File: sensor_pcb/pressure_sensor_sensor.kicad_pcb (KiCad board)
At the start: 2 copper layers, 34 x 34 mm, 12 parts, among them J1 Conn_01x01_Pin, J10 Conn_01x02_Pin, J12 Conn_01x01_Pin, J13 Conn_01x01_Pin, J14 Conn_01x01_Pin, J15 Conn_01x01_Pin, J16 Conn_01x01_Pin, J17 Conn_01x01_Pin, J18 Conn_01x01_Pin, J7 Conn_01x02_Pin, J8 Conn_01x02_Pin, J9 Conn_01x02_Pin

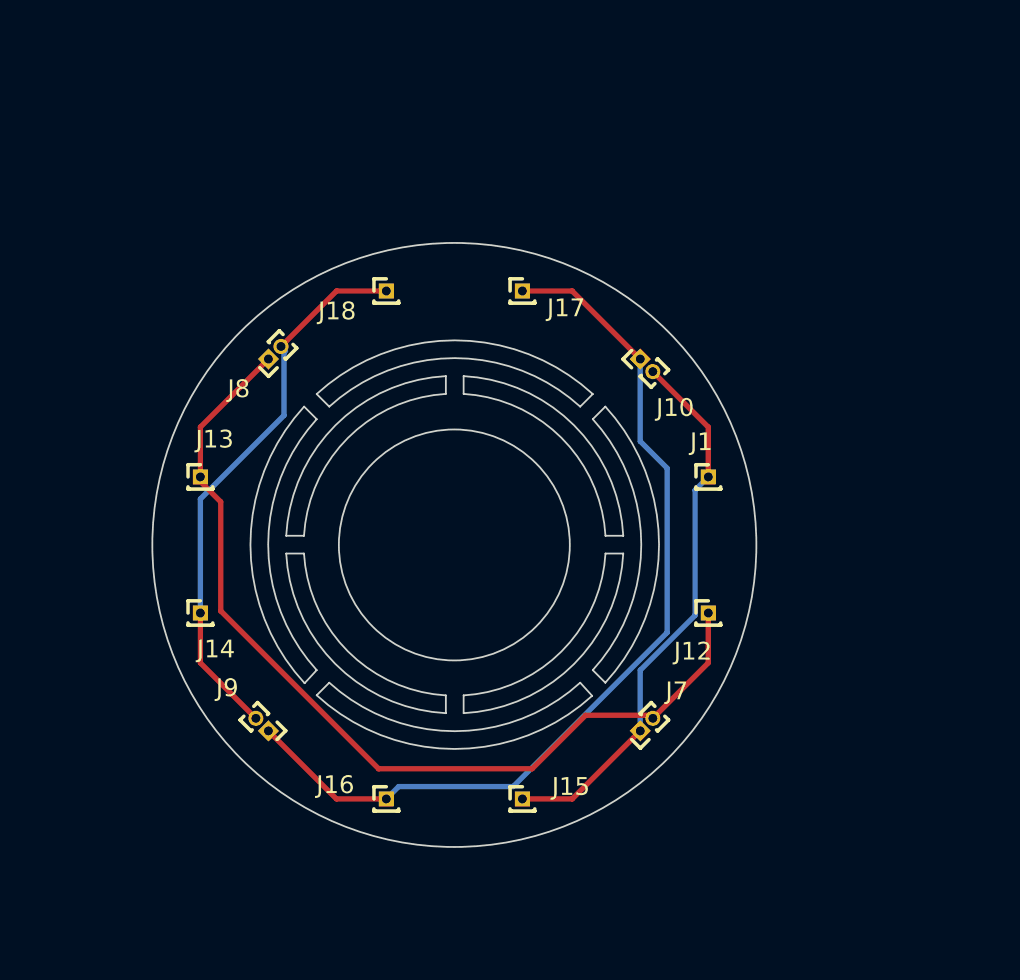
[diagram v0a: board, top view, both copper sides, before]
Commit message: mounting_holes_added
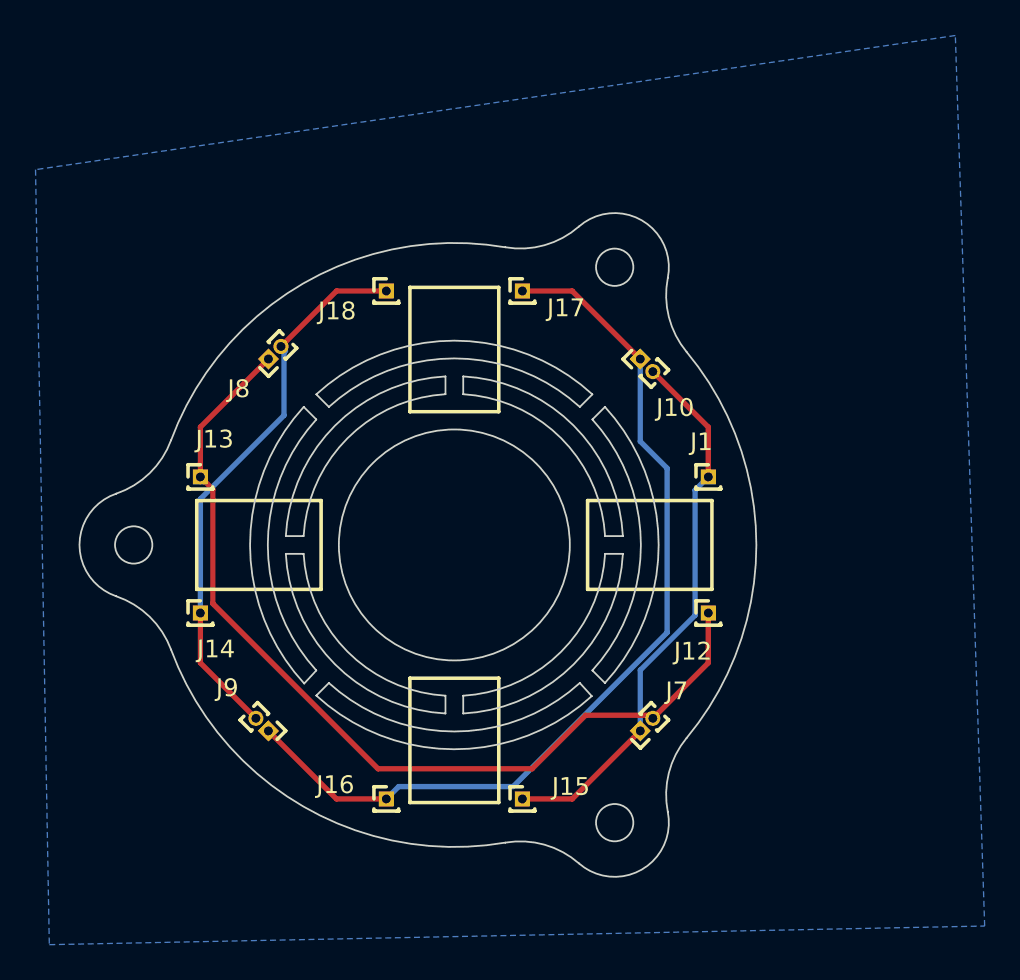
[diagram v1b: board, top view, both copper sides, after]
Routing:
- added copper zone on B.Cu, net GNDA
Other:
- board size 34 x 34 mm -> 38.1 x 37.4 mm

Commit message: alignement_corrected
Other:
- outline, holes or cut-outs redrawn
- board text added: "+3.3V"
- board text added: "A+"
- board text added: "A-"
- board text added: "GND"

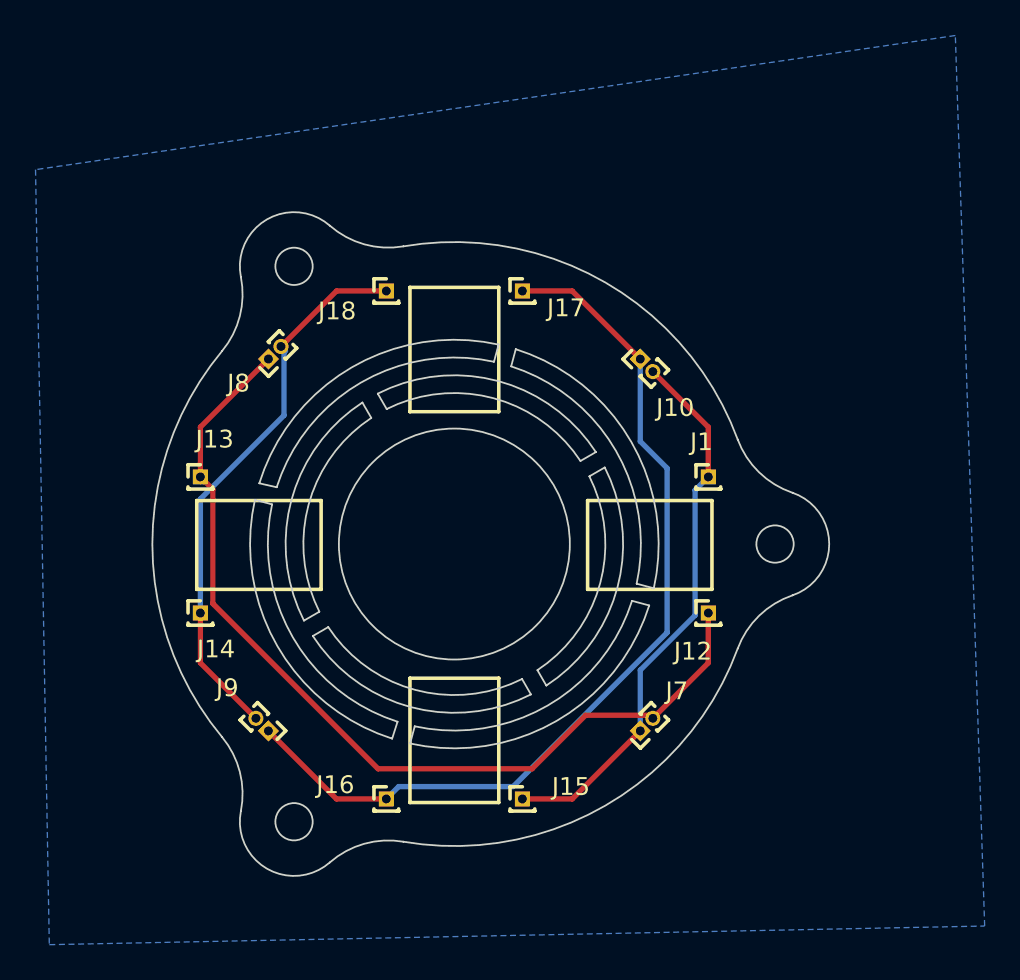
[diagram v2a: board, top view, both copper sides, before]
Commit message: 3d_start_point_added
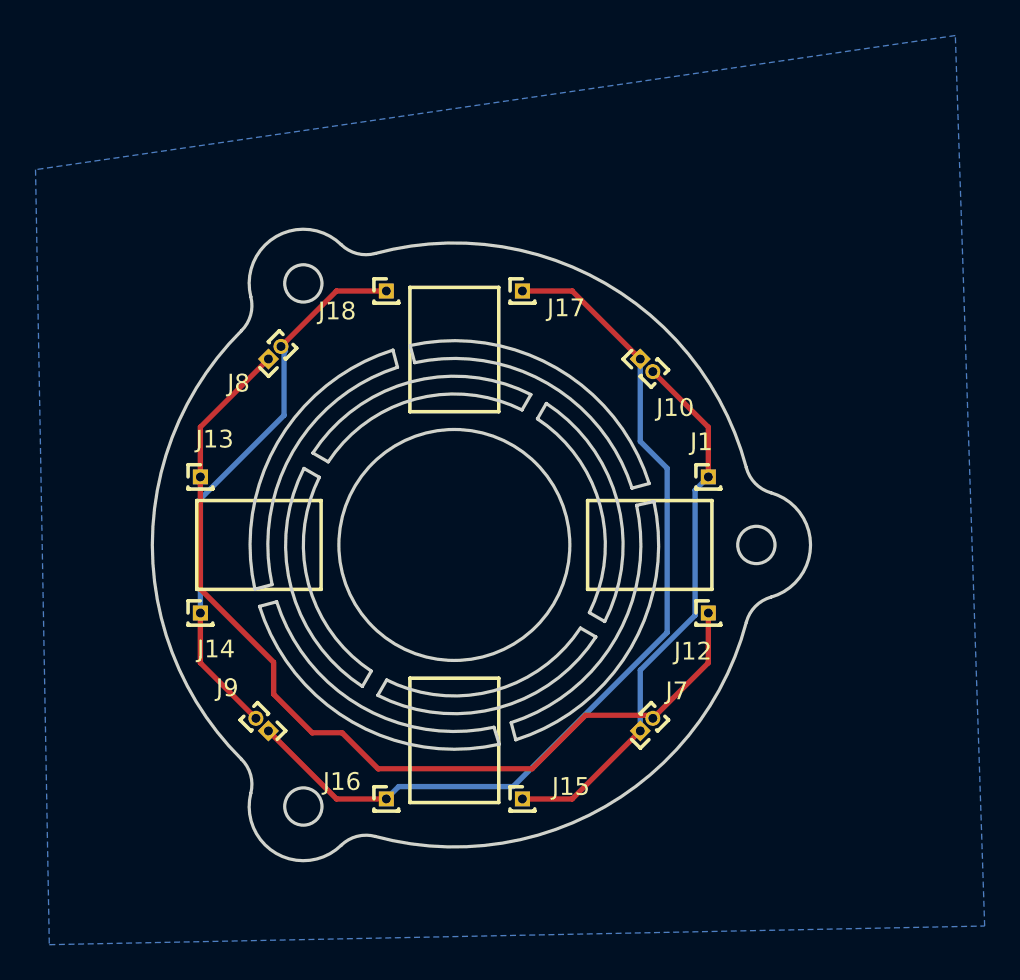
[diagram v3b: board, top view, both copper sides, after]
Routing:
- net /Ap: track 53.1 -> 53.8 mm
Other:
- board size 38.1 x 37.4 mm -> 37.1 x 35.5 mm
